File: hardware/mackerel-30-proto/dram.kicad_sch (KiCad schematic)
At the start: 16 parts, among them J11 Conn_02x05_Odd_Even, U10 SIMM72, U9 EPM7128, X3 CXO_DIP14

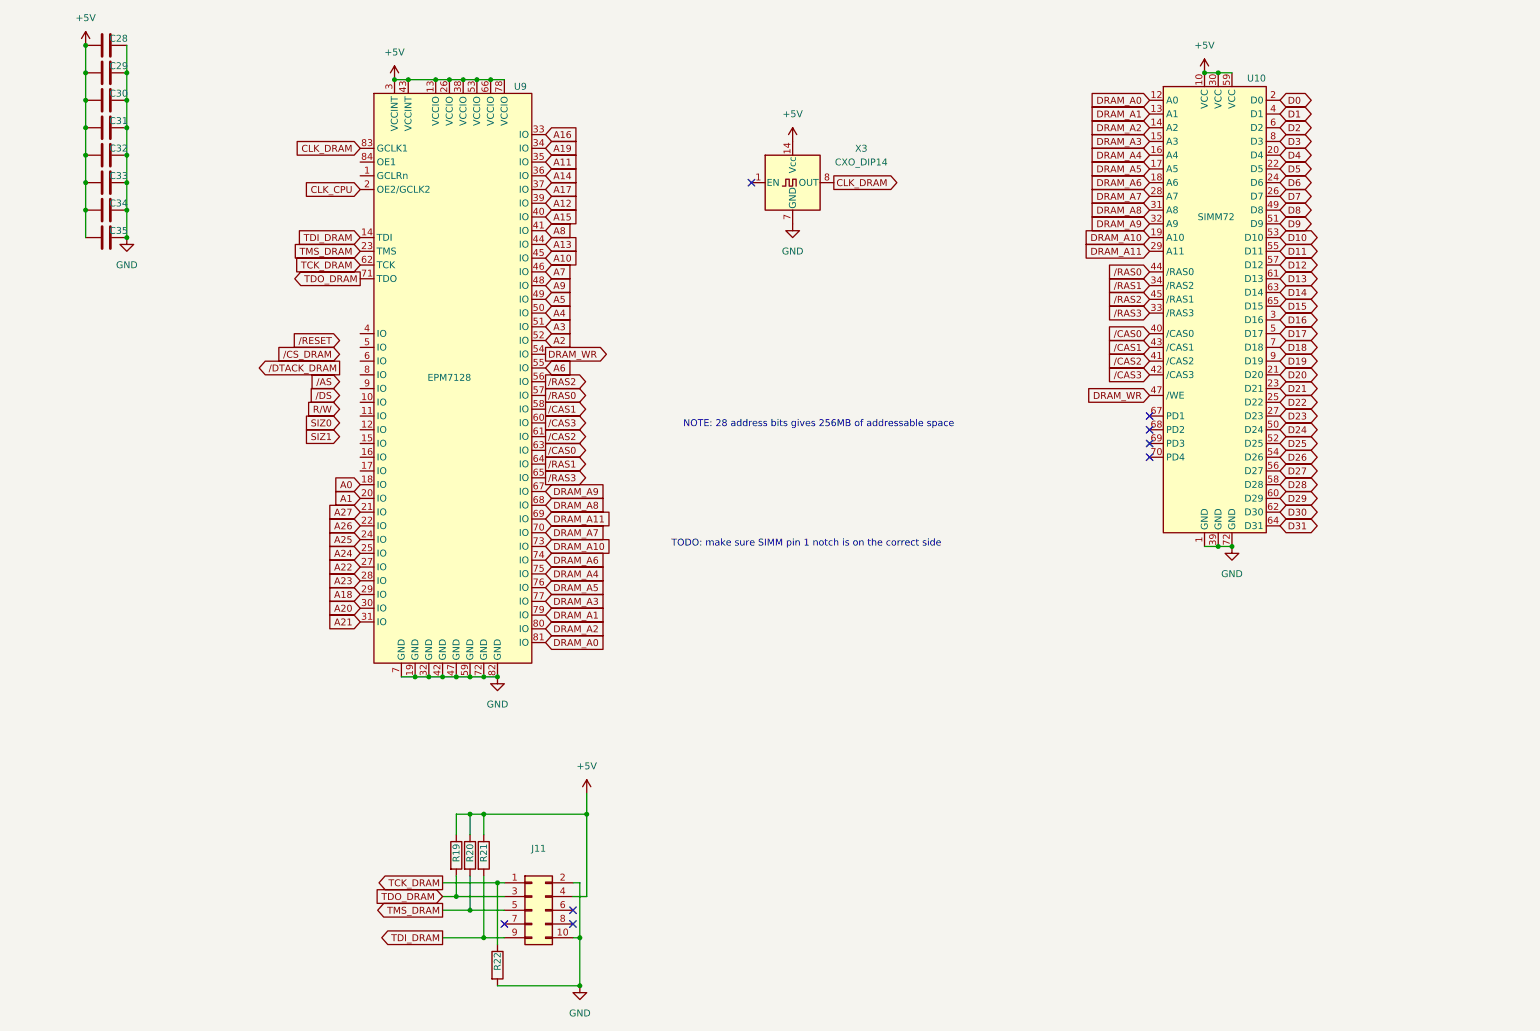
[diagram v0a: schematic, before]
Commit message: Roughly routed all but expansion and reset
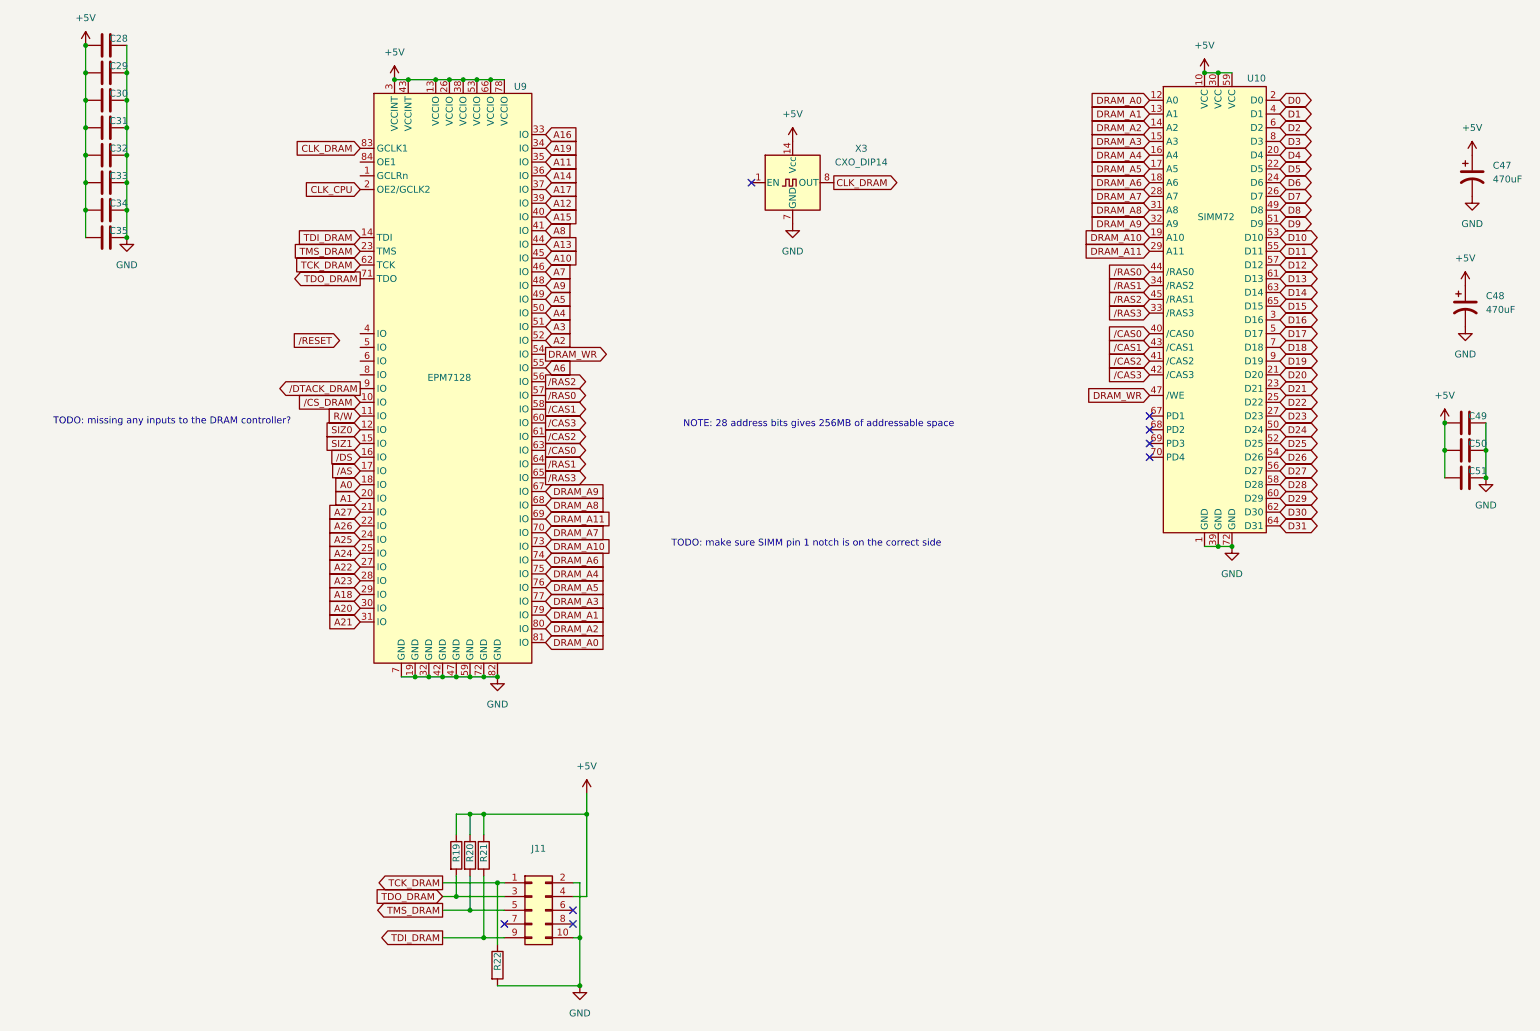
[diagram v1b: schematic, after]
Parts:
- added C47, C48: 470uF, Capacitor_THT:CP_Radial_D8.0mm_P3.50mm, symbol Device:C_Polarized_US
- added C49, C50, C51: 0.1uF, Capacitor_THT:C_Disc_D4.3mm_W1.9mm_P5.00mm, symbol Device:C
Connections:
- net +5V: now also C47.1, C48.1, C49.1, C50.1, C51.1
- net GND: now also C47.2, C48.2, C49.2, C50.2, C51.2
- net R/W: now also U9.11 (IO)
- net SIZ0: now also U9.12 (IO)
- net SIZ1: now also U9.15 (IO)
- net /AS: now also U9.17 (IO)
- net /CS_DRAM: now also U9.10 (IO)
- net /DS: now also U9.16 (IO)
- net /DTACK_DRAM: now also U9.9 (IO)
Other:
- note added: "TODO: missing any inputs to the DRAM controller?"

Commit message: Mack-30 routed except for expansion header
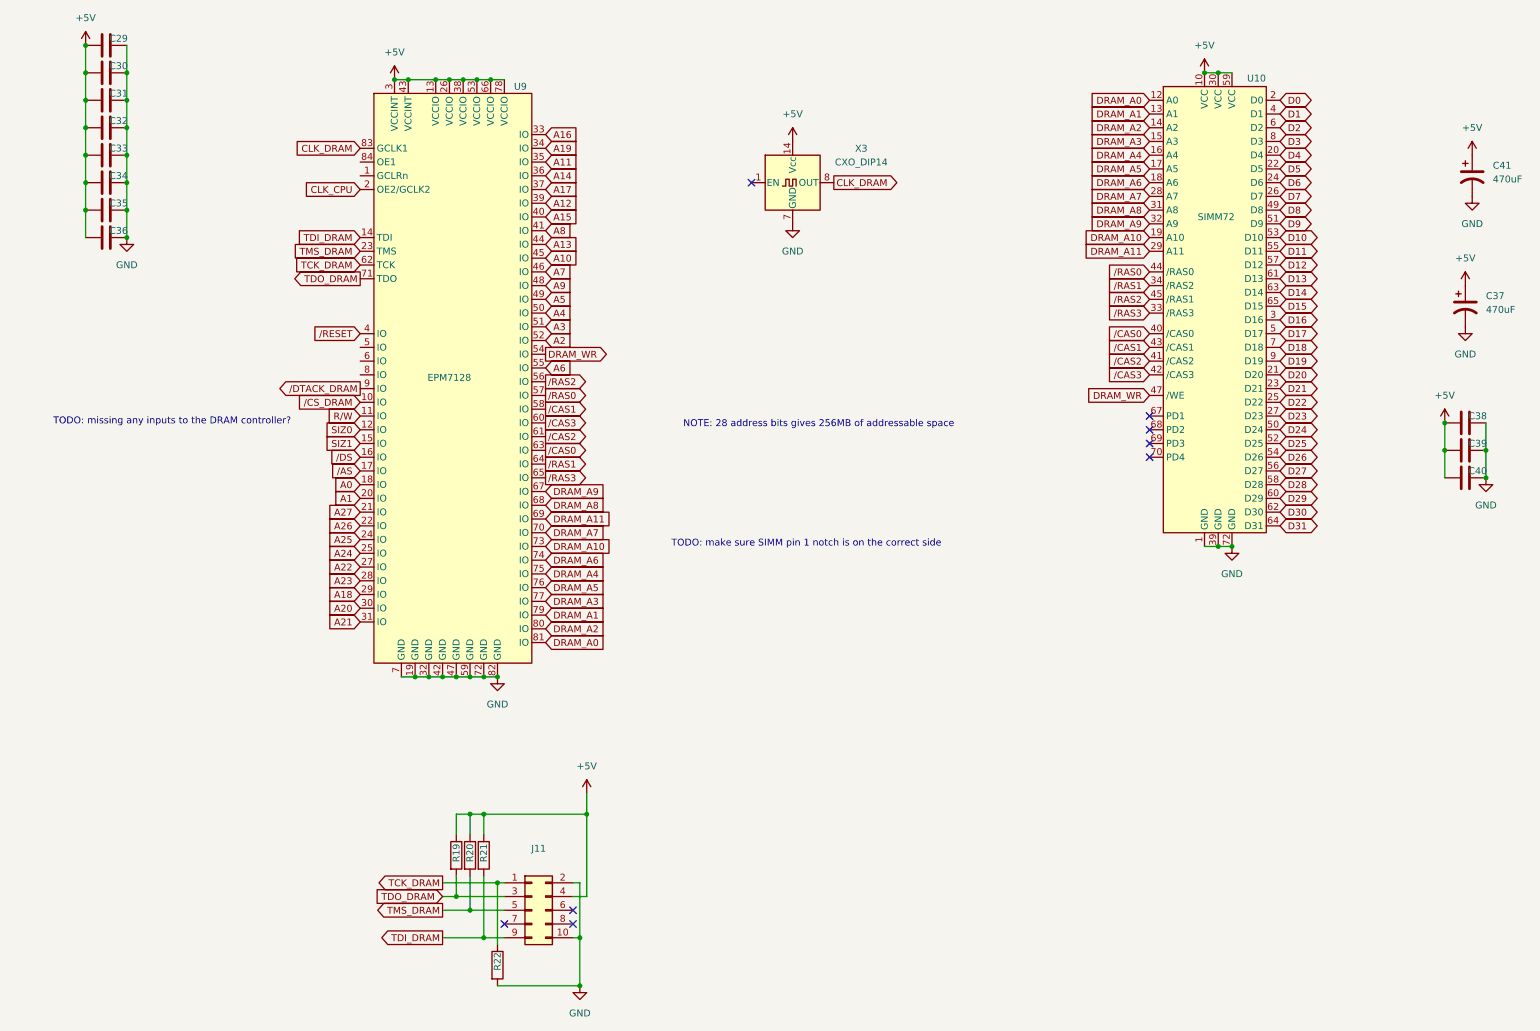
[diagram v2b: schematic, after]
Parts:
- renumbered C28 to C29, C29 to C30, C30 to C31, C31 to C32, C32 to C33, C33 to C34, C34 to C35, C35 to C36, C48 to C37, C49 to C38, C50 to C39, C51 to C40, C47 to C41
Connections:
- net /RESET: now also U9.4 (IO)

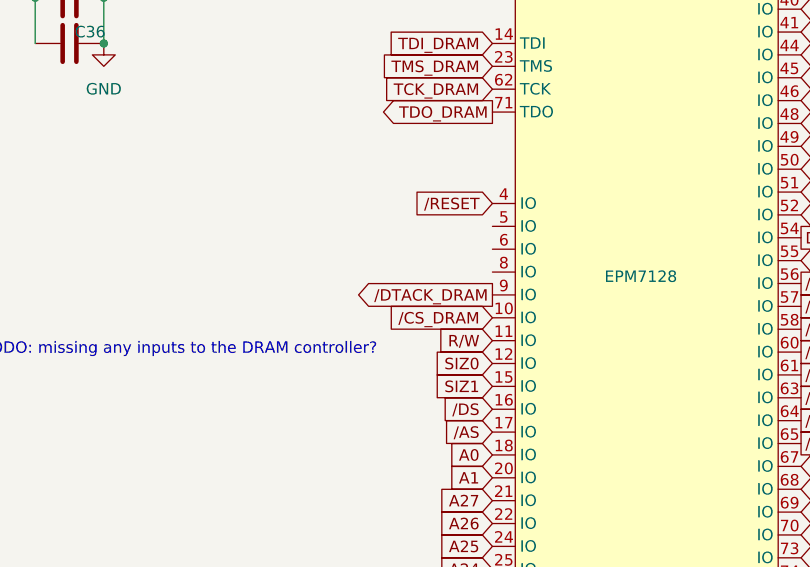
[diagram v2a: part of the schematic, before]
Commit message: Expansion header routed
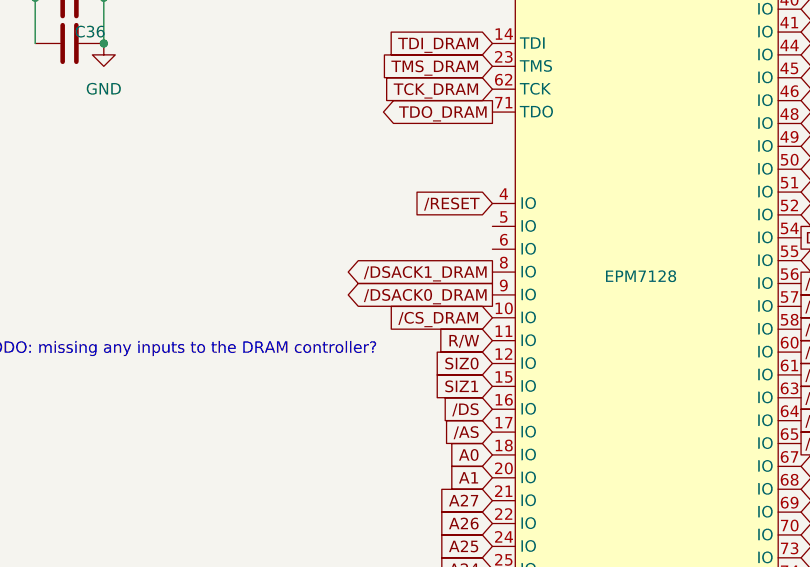
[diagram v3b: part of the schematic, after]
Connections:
- net /DSACK1_DRAM: now reaches U9.8 (IO)
- net /DTACK_DRAM renamed /DSACK0_DRAM
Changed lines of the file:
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@@
 		)
 	)
-	(global_label "{slash}DTACK_DRAM"
+	(global_label "{slash}DSACK0_DRAM"
 		(shape output)
 		(at 29.21 80.01 180)
@@
 		)
 		(property "Intersheetrefs" "${INTERSHEET_REFS}"
-			(at 12.9805 80.01 0)
+			(at 11.5291 80.01 0)
 			(effects
 				(font
@@
 				(hide yes)
 			)
+		)
+	)
+	(global_label "{slash}DSACK1_DRAM"
+		(shape output)
+		(at 29.21 77.47 180)
+		(fields_autoplaced yes)
+		(effects
+			(font
+				(size 1.27 1.27)
+			)
+			(justify right)
+		)
+		(property "Intersheetrefs" "${INTERSHEET_REFS}"
+			(at 11.5291 77.47 0)
+			(effects
+				(font
+					(size 1.27 1.27)
+				)
+				(justify right)
+				(hide yes)
+			)

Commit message: PCB cleanup
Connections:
- net GND: now also U9.1 (GCLRn), U9.84 (OE1)
- no-connect marks 8 -> 10
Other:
- note removed: "TODO: missing any inputs to the DRAM controller?"
- title: Mackerel-30 Proto -> Mackerel-30
- moved on the sheet: C29, C30, C31, C32, C33, C34, C35, C36, U9

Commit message: Mackerel-30 v0.1 PCB release
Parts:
- R19, R20, R21, R22: value R -> 4k7
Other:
- note removed: "TODO: make sure SIMM pin 1 notch is on the correct side"
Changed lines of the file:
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@@
 		)
 	)
-	(text "TODO: make sure SIMM pin 1 notch is on the correct side"
-		(exclude_from_sim no)
-		(at 119.126 102.616 0)
-		(effects
-			(font
-				(size 1.27 1.27)
-			)
-		)
-	)
 	(global_label "{slash}CAS3"
 		(shape output)
@@
 			)
 		)
-		(property "Value" "R"
+		(property "Value" "4k7"
 			(at 52.07 167.6399 0)
 			(effects
@@
 			)
 		)
-		(property "Value" "R"
+		(property "Value" "4k7"
 			(at 54.61 167.6399 0)
 			(effects
@@
 			)
 		)
-		(property "Value" "R"
+		(property "Value" "4k7"
 			(at 57.15 187.9599 0)
 			(effects
@@
 			)
 		)
-		(property "Value" "R"
+		(property "Value" "4k7"
 			(at 49.53 167.6399 0)
 			(effects
